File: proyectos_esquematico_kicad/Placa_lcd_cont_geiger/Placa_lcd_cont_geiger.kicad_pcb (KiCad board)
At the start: 2 copper layers, 68.6 x 53.3 mm, 18 parts, among them J1 Conn_02x04_Counter_Clockwise, J2 Conn_01x14_Female, J3 Conn_01x05_Female, P1 Power, P2 Analog, P3 Digital, P4 Digital, Q1 BC548, Q2 BC548, Q3 BC558

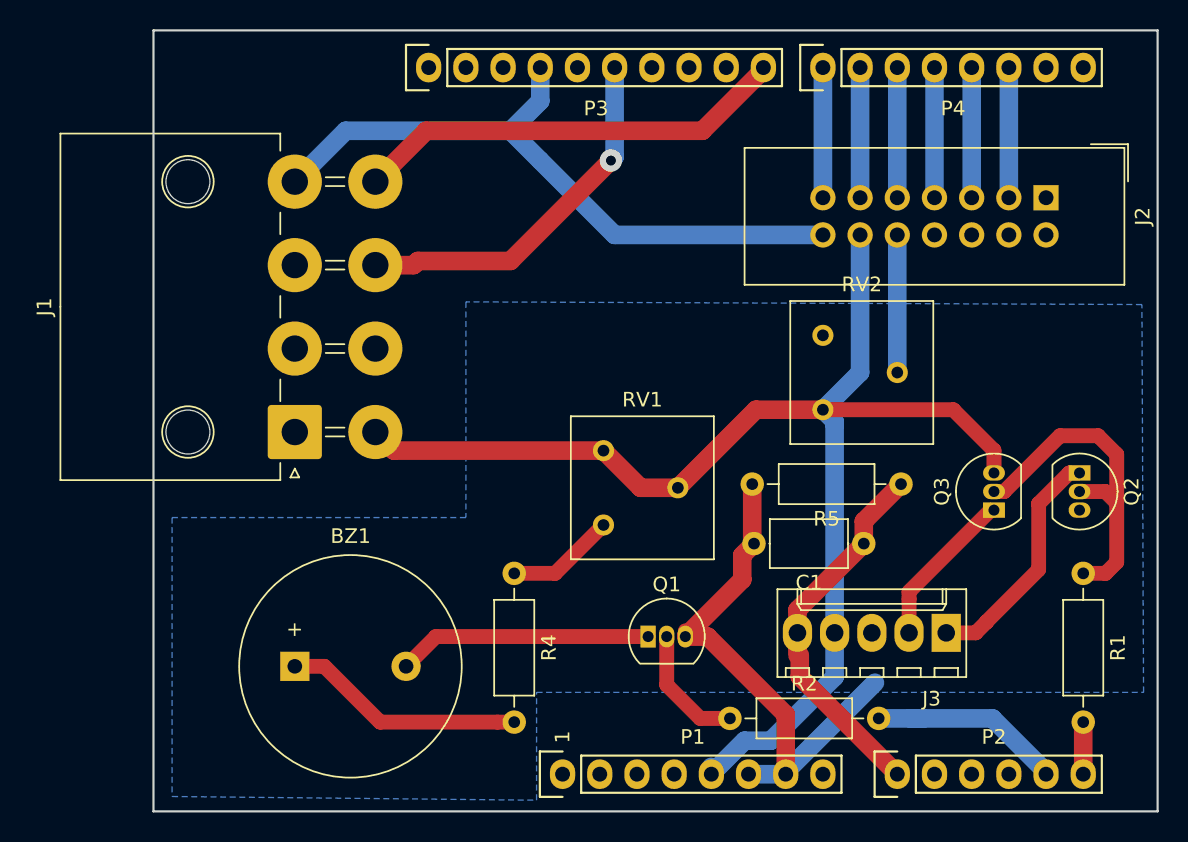
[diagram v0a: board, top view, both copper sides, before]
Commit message: Modificaciones en el PCB para poder mardarlo a hacer al LCI. Agregado del esquematico del Arduino UNO R3 actualizado a la carpeta 'doc'
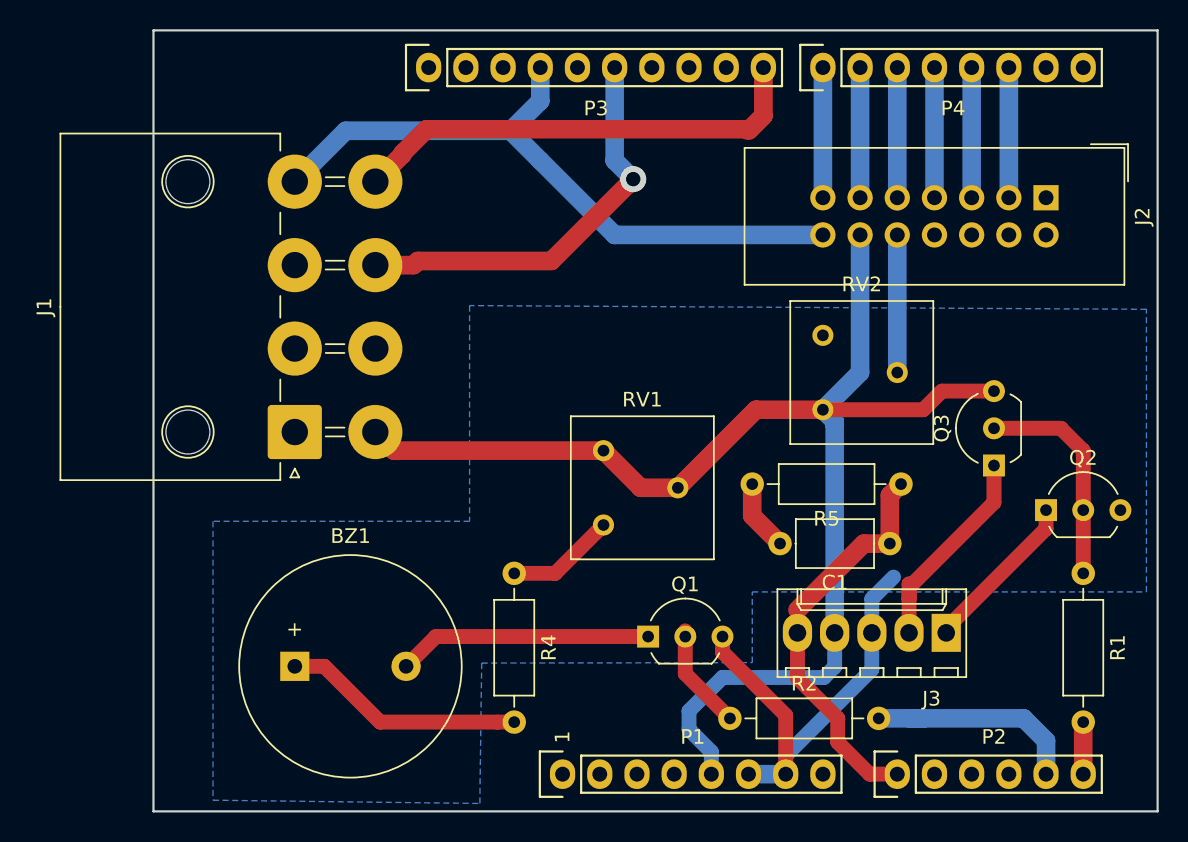
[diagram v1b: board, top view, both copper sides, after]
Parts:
- Q1, Q2, Q3: footprint Package_TO_SOT_THT:TO-92_Inline -> Package_TO_SOT_THT:TO-92_Inline_Wide
- moved Q2 3.42 mm to (172.0, 105.8), turned to 0 degrees
- moved Q3 3.05 mm to (168.4, 102.7)
- moved C1 1.78 mm to (161.3, 108.1)
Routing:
- net Net-(Q2-Pad2): track 23.3 -> 15.1 mm
- net Net-(J3-Pad1): track 16.3 -> 11.2 mm
- net /8: track 29.8 -> 33.3 mm
- net /12(MISO): track 25.4 -> 28.4 mm
- net Net-(J3-Pad2): track 10.9 -> 13.7 mm
- net /A0: track 25.7 -> 27.9 mm
- net GND: track 83.0 -> 81.2 mm
- net VCC: track 92.1 -> 94.0 mm
- net /A4: track 14.0 -> 15.4 mm
- net Net-(Q1-Pad2): track 8.57 -> 7.33 mm
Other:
- net class Default: clearance 0.2 -> 0.6096; trace_width 0.25 -> 0.508; via_dia 0.6 -> 1.778; via_drill 0.4 -> 0.9906
- rule trace_clearance: 0.2 -> 0.6096
- rule trace_min: 0.2 -> 0.4064

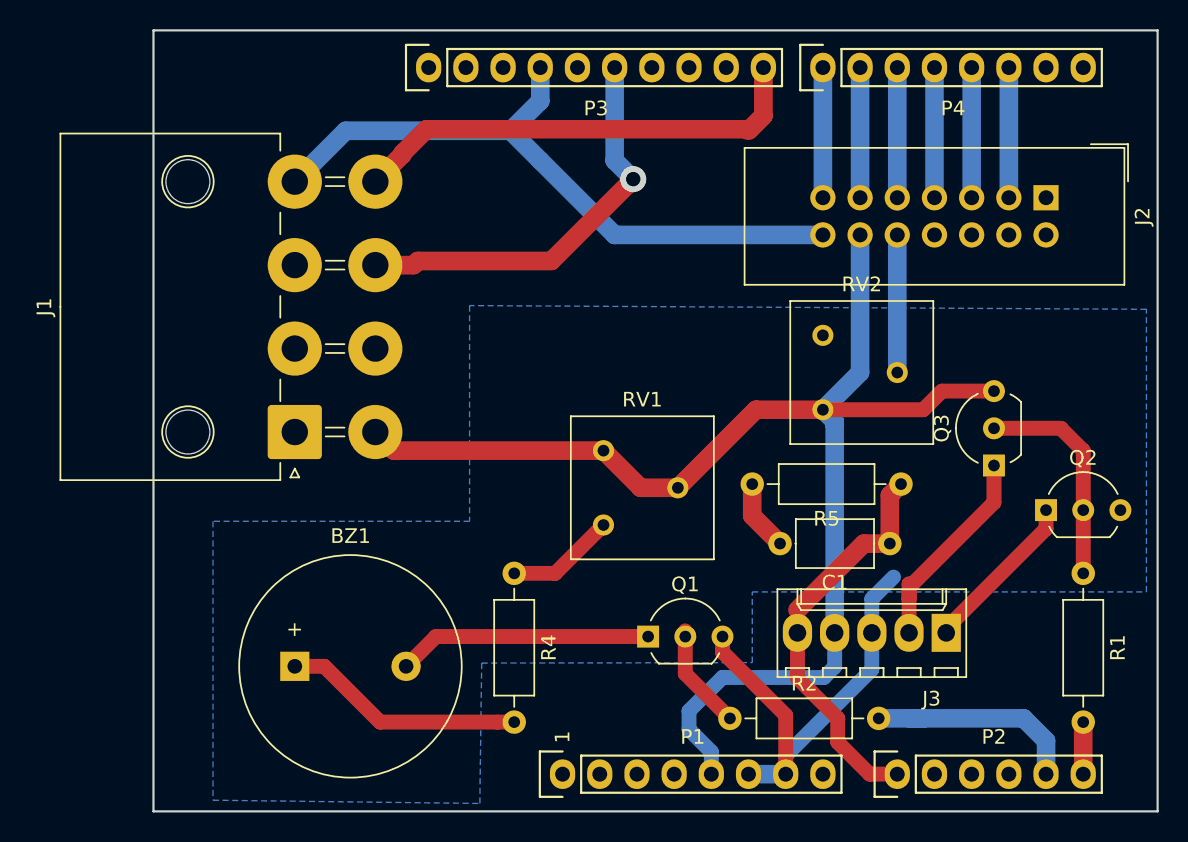
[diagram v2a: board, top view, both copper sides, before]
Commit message: Cambios menores en el shield para adaptarlo a los cambios hechos sobre el prototipo
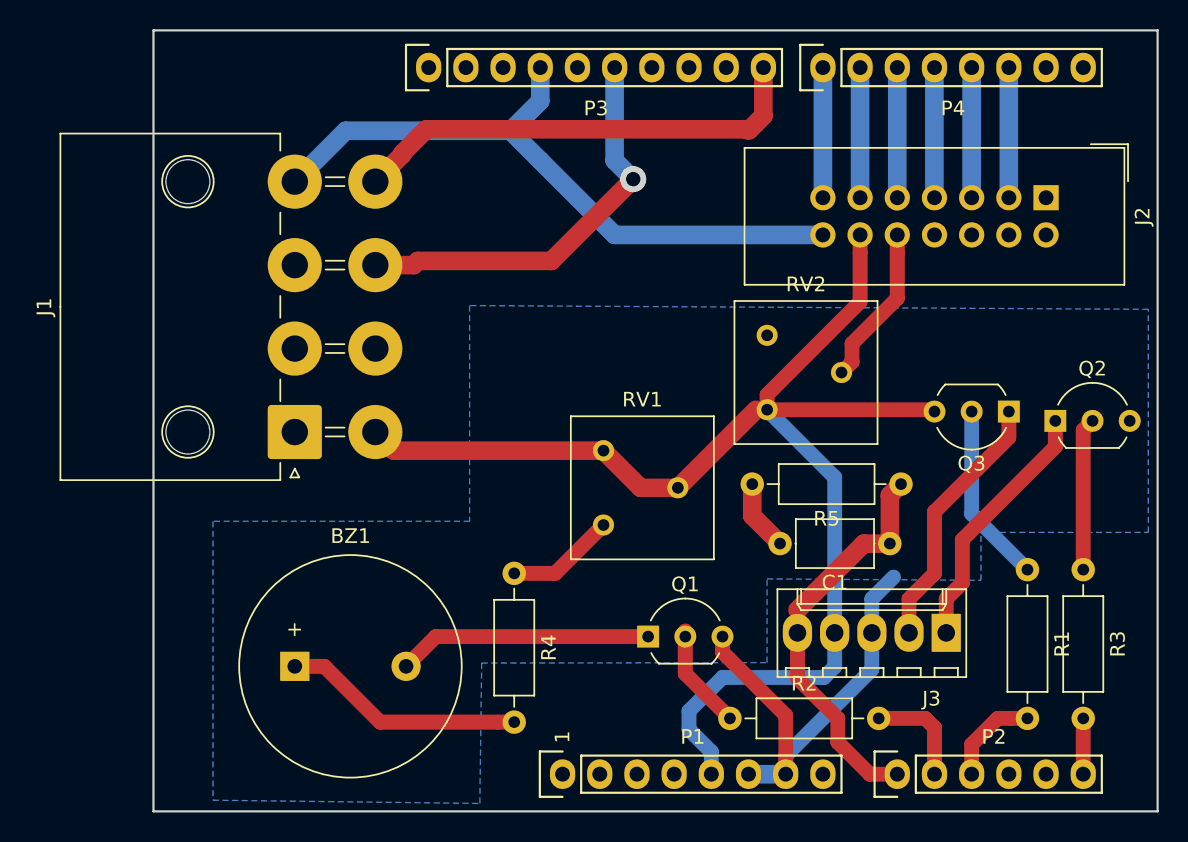
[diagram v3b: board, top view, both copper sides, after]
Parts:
- added R3: 10k, Resistor_THT:R_Axial_DIN0207_L6.3mm_D2.5mm_P10.16mm_Horizontal, F.Cu at (174.5, 109.9)
- moved Q2 6.13 mm to (172.6, 99.7)
- moved Q3 3.82 mm to (169.4, 99.1), turned to 180 degrees
- moved R1 3.82 mm to (170.7, 109.9)
- moved RV2 3.81 mm to (152.9, 98.9)
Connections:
- Q3 pad 2: Net-(Q2-Pad2) -> Net-(Q3-Pad2)
- R1 pad 1: Net-(Q2-Pad2) -> Net-(Q3-Pad2)
- R1 pad 2: /A5 -> /A2
- R2 pad 2: /A4 -> /A1
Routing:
- net /A4: track 15.4 -> 0.15 mm
- net Net-(Q3-Pad2): track 0.00 -> 12.4 mm
- net /A1: track 0.00 -> 7.25 mm
- net Net-(J3-Pad1): track 11.2 -> 17.9 mm
- net /A2: track 0.00 -> 6.58 mm
- net Net-(Q2-Pad2): track 15.1 -> 10.4 mm
- net Net-(J3-Pad2): track 13.7 -> 17.9 mm
- net VCC: track 94.0 -> 92.4 mm
- net Net-(J2-Pad10): track 9.40 -> 11.0 mm
